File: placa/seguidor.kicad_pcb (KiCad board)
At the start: 2 copper layers, 50 x 58 mm, 20 parts, among them J1 conn_bat, J2 conn_sensores, J3 conn_motor, J4 conn_pwm, SW2 btn_arranque, U1 ATmega328P-P, U2 LM7805_TO220, Y1 Crystal

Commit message: placa: agrego conector ICSP, protección de alimentación, botón de reset
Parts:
- added D2: 1N4007, Diode_THT:D_DO-41_SOD81_P10.16mm_Horizontal, F.Cu at (41.1, 40.4)
- added J5: conn_icsp, Connector_PinHeader_2.54mm:PinHeader_2x03_P2.54mm_Vertical, F.Cu at (47.3, 61.2)
- added SW3: btn_reset, Button_Switch_THT:SW_PUSH_6mm_H5mm, F.Cu at (43.2, 48.7)
- moved C3 9.40 mm to (81.2, 40.6)
- moved C2 9.40 mm to (97.7, 40.6)
- moved U2 9.40 mm to (86.9, 40.6)
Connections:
- C3 pad 1: +BATT -> Net-(D2-K)
- U1 pad 16: unconnected-(U1-PB2-Pad16) -> led_largada
- U1 pad 17: unconnected-(U1-PB3-Pad17) -> mosi
- U1 pad 18: unconnected-(U1-PB4-Pad18) -> miso
- U1 pad 19: led_largada -> sck
- U2 pad 1: +BATT -> Net-(D2-K)
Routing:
- net +5V: track 132.4 -> 105.8 mm
- net led_largada: track 18.9 -> 0.00 mm
- net +BATT: track 21.3 -> 5.47 mm
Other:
- board text added: "LFO BIC"

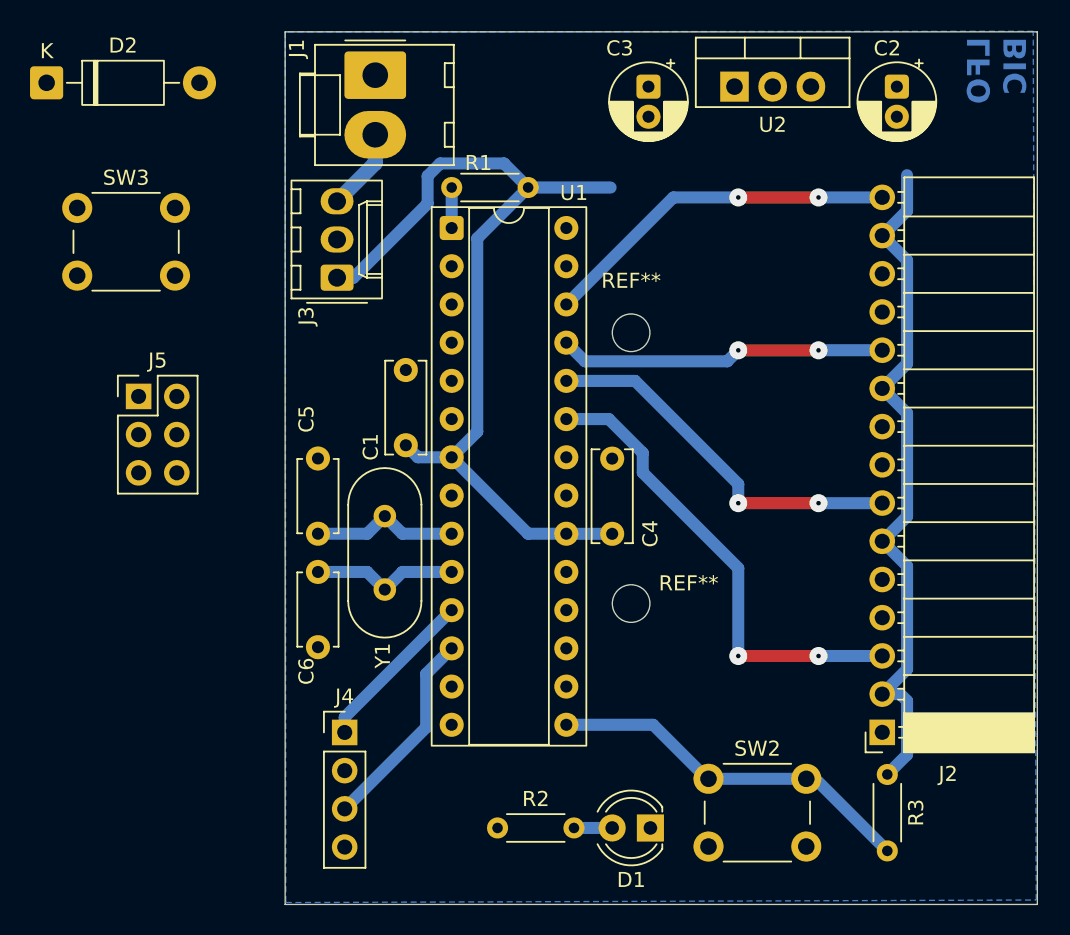
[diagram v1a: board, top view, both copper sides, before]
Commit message: placa reordenada y conector spi
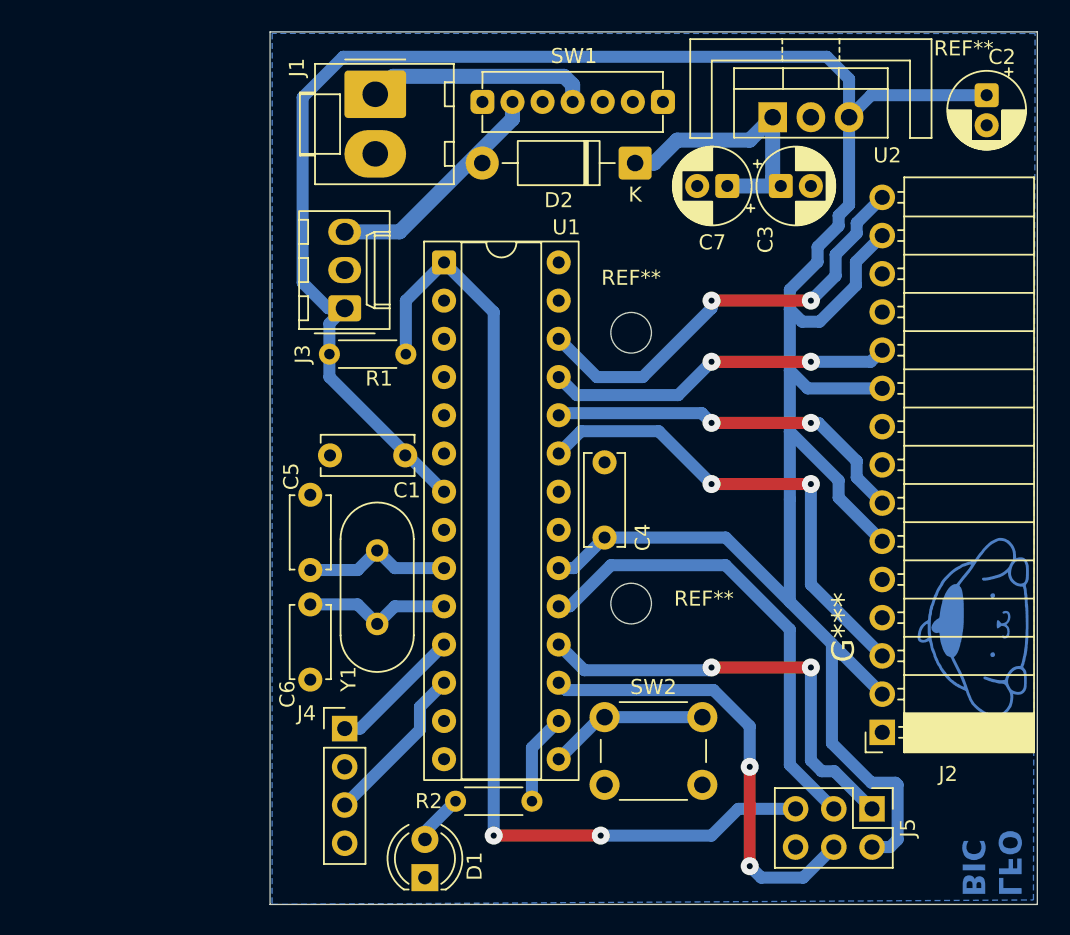
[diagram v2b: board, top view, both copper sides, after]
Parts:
- removed R3: 3.3k, Resistor_THT:R_Axial_DIN0204_L3.6mm_D1.6mm_P5.08mm_Horizontal
- removed the REF** at (80.0, 57.0)
- removed the REF** at (80.0, 75.0)
- removed SW3: btn_reset, Button_Switch_THT:SW_PUSH_6mm_H5mm
- added C7: 100u, Capacitor_THT:CP_Radial_D5.0mm_P2.00mm, F.Cu at (86.4, 47.2)
- added G***: LOGO, Custom:pompompurin, F.Cu at (102.7, 76.6)
- added REF**: MountingHole_2.7mm, MountingHole:MountingHole_2.7mm, F.Cu at (80.0, 75.0)
- added REF**: MountingHole_2.7mm, MountingHole:MountingHole_2.7mm, F.Cu at (80.0, 57.0)
- added REF**: Disipador, Custom:Heatsink_Custom, F.Cu at (91.9, 37.6)
- added SW1: SW_custom, Custom:Switch custom, F.Cu at (72.1, 41.7)
- D2: value 1N4007 -> 1N5819
- moved J5 55.9 mm to (96.0, 88.6), turned to -90 degrees
- moved D2 39.5 mm to (80.3, 45.7), turned to 180 degrees
- moved R1 17.2 mm to (59.9, 58.4), turned to 0 degrees
- moved D1 15.3 mm to (66.3, 93.2), turned to 90 degrees
- moved C3 11.0 mm to (89.9, 47.2), turned to 0 degrees
- moved SW2 8.03 mm to (78.2, 82.5)
- moved C2 6.00 mm to (103.6, 41.2)
- moved U2 3.25 mm to (89.4, 42.7)
- moved R2 2.90 mm to (73.4, 88.1), turned to 180 degrees
- moved C5 2.47 mm to (58.7, 72.8)
- moved U1 2.34 mm to (67.6, 52.3)
- moved Y1 2.34 mm to (63.1, 71.5)
- moved C6 2.22 mm to (58.7, 75.1)
- moved J3 2.09 mm to (61.0, 55.4)
- moved J1 1.27 mm to (63.0, 41.1)
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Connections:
- net Net-(D2-K) renamed V_IN
- D2 pad 2: +BATT -> VCC
- J1 pad 1: GND -> +BATT
- J1 pad 2: +BATT -> GND
- J3 pad 3: +BATT -> VCC
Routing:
- net +5V: track 105.8 -> 186.3 mm
- net reset: track 2.69 -> 67.4 mm, vias 0 -> 2
- net sck: track 0.00 -> 31.4 mm
- net mosi: track 0.00 -> 29.9 mm, vias 0 -> 2
- net miso: track 0.00 -> 29.1 mm, vias 0 -> 2
- net V_IN: track 0.00 -> 18.8 mm
- net VCC: track 0.00 -> 15.4 mm
- net arranque: track 24.8 -> 10.7 mm
- net +BATT: track 5.47 -> 15.0 mm
- net led_largada: track 0.00 -> 6.07 mm
- net sensor1: track 24.0 -> 29.1 mm
- net motor_der: track 13.6 -> 10.9 mm
- net motor_izq: track 11.1 -> 8.92 mm
- net sensor2: track 21.8 -> 23.2 mm
- net Net-(D1-A): track 2.54 -> 3.38 mm
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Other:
- board size 50 x 58 mm -> 51 x 58 mm

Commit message: pins cambiados. PID ajustado. mensajes de debug.
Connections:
- net arranque renamed boton_largada
- net led_largada renamed led_arranque
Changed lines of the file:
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@@
 			(layers "*.Cu" "*.Mask")
 			(remove_unused_layers no)
-			(net "arranque")
+			(net "boton_largada")
 			(pinfunction "PB1_15")
 			(pintype "bidirectional")
@@
 			(layers "*.Cu" "*.Mask")
 			(remove_unused_layers no)
-			(net "led_largada")
+			(net "led_arranque")
 			(pinfunction "PB2_16")
 			(pintype "bidirectional")
@@
 			(layers "*.Cu" "*.Mask")
 			(remove_unused_layers no)
-			(net "led_largada")
+			(net "led_arranque")
 			(pintype "passive")
 		)
@@
 			(layers "*.Cu" "*.Mask")
 			(remove_unused_layers no)
-			(net "arranque")
+			(net "boton_largada")
 			(pinfunction "1_1")
 			(pintype "passive")
@@
 			(layers "*.Cu" "*.Mask")
 			(remove_unused_layers no)
-			(net "arranque")
+			(net "boton_largada")
 			(pinfunction "1_1")
 			(pintype "passive")
@@
 	)
 	(segment
-		(start 77.978 82.55)
-		(end 75.184 85.344)
-		(width 0.8)
-		(layer "B.Cu")
-		(net "arranque")
-	)
-	(segment
-		(start 84.732 82.55)
-		(end 77.978 82.55)
-		(width 0.8)
-		(layer "B.Cu")
-		(net "arranque")
-	)
-	(segment
-		(start 73.406 84.582)
-		(end 73.406 88.138)
-		(width 0.8)
-		(layer "B.Cu")
-		(net "led_largada")
-	)
-	(segment
-		(start 75.184 82.804)
-		(end 73.406 84.582)
-		(width 0.8)
-		(layer "B.Cu")
-		(net "led_largada")
-	)
-	(segment
 		(start 85.344 67.056)
 		(end 91.948 67.056)
@@
 		(net "sensor1")
 	)
+	(segment
+		(start 73.406 84.582)
+		(end 73.406 88.138)
+		(width 0.8)
+		(layer "B.Cu")
+		(net "led_arranque")
+	)
+	(segment
+		(start 75.184 82.804)
+		(end 73.406 84.582)
+		(width 0.8)
+		(layer "B.Cu")
+		(net "led_arranque")
+	)
+	(segment
+		(start 77.978 82.55)
+		(end 75.184 85.344)
+		(width 0.8)
+		(layer "B.Cu")
+		(net "boton_largada")
+	)
+	(segment
+		(start 84.732 82.55)
+		(end 77.978 82.55)
+		(width 0.8)
+		(layer "B.Cu")
+		(net "boton_largada")
+	)
 	(zone
